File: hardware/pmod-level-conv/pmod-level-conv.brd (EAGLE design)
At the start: 23 x 18.5 mm, 6 parts, among them J1 PMOD_PLUG1, J2 PMOD_SOCKET1, J3 VCC, U1 TXB0108PWR

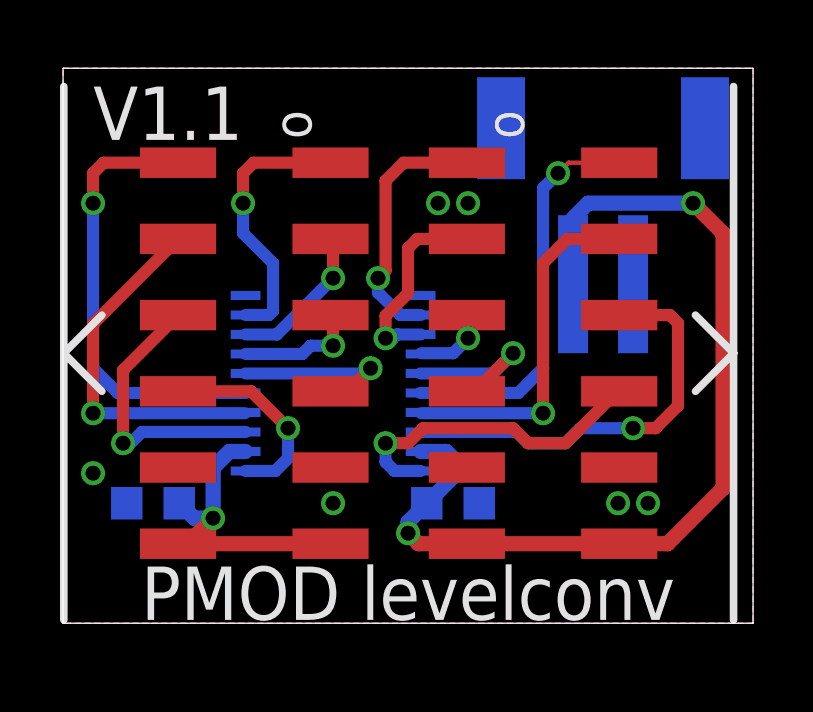
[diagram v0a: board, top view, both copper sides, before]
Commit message: pmod-level-conv : fixed NC OE
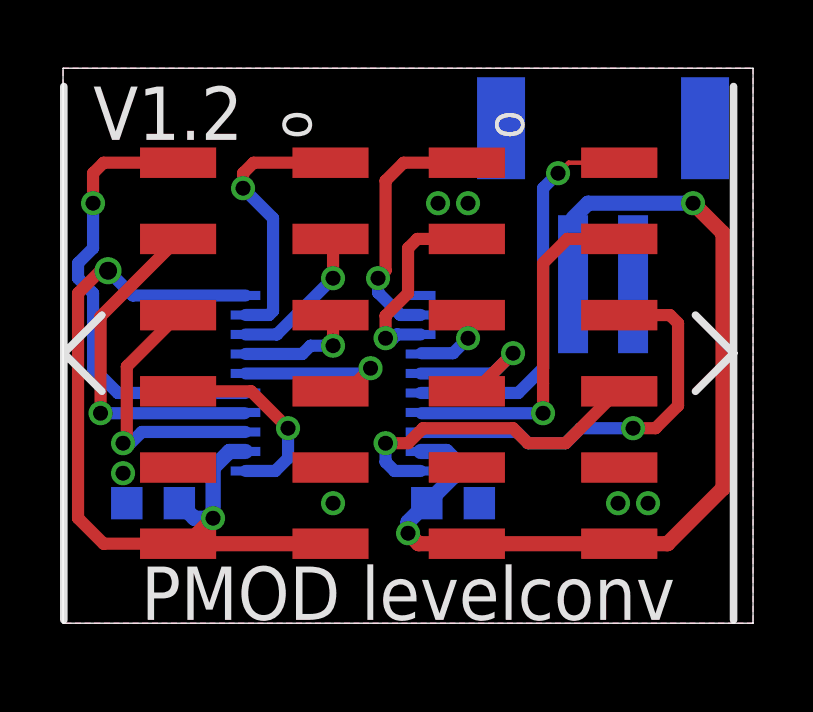
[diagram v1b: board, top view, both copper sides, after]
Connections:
- net VCCIO: now also U1.10
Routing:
- net VCCIO: track 10.9 -> 28.3 mm, vias 1 -> 2
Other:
- board text added: "V1.2"
- board text removed: "V1.1"
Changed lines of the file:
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@@
 <wire x1="0" y1="18.5" x2="0" y2="0" width="0" layer="20"/>
 <text x="11.5" y="1" size="1.778" layer="21" font="vector" align="center">PMOD levelconv</text>
-<text x="3.5" y="17" size="1.778" layer="21" font="vector" align="center">V1.1</text>
+<text x="3.5" y="17" size="1.778" layer="21" font="vector" align="center">V1.2</text>
 </plain>
 <attributes>
@@
 <vertex x="0" y="0"/>
 </polygon>
-<via x="1" y="5" extent="1-16" drill="0.5" shape="octagon"/>
+<via x="2" y="5" extent="1-16" drill="0.5" shape="octagon"/>
 <via x="9" y="4" extent="1-16" drill="0.5" shape="octagon"/>
 <via x="19.5" y="4" extent="1-16" drill="0.5" shape="octagon"/>
@@
 <wire x1="5" y1="3.5" x2="5" y2="5.1793125" width="0.508" layer="16"/>
 <wire x1="5.5456875" y1="5.725" x2="6.0822" y2="5.725" width="0.508" layer="16"/>
+<contactref element="U1" pad="10"/>
+<wire x1="6.0822" y1="10.925" x2="2.325" y2="10.925" width="0.4064" layer="16"/>
+<wire x1="2.325" y1="10.925" x2="1.5" y2="11.75" width="0.4064" layer="16"/>
+<via x="1.5" y="11.75" extent="1-16" drill="0.6" shape="octagon"/>
+<wire x1="1.5" y1="11.75" x2="1.25" y2="11.75" width="0.4064" layer="1"/>
+<wire x1="1.25" y1="11.75" x2="0.5" y2="11" width="0.4064" layer="1"/>
+<wire x1="0.5" y1="11" x2="0.5" y2="3.5" width="0.4064" layer="1"/>
+<wire x1="3.835" y1="2.65" x2="1.35" y2="2.65" width="0.4064" layer="1"/>
+<wire x1="1.35" y1="2.65" x2="0.5" y2="3.5" width="0.4064" layer="1"/>
 </signal>
 <signal name="VCC">
@@
 <wire x1="6.0822" y1="6.375" x2="2.625" y2="6.375" width="0.4064" layer="16"/>
 <via x="2" y="6" extent="1-16" drill="0.5" shape="octagon"/>
-<wire x1="2" y1="6" x2="2" y2="8.435" width="0.4064" layer="1"/>
-<wire x1="2" y1="8.435" x2="3.835" y2="10.27" width="0.4064" layer="1"/>
+<wire x1="2" y1="6" x2="2.125" y2="6.125" width="0.4064" layer="1"/>
+<wire x1="2.125" y1="6.125" x2="2.125" y2="8.56" width="0.4064" layer="1"/>
+<wire x1="2.125" y1="8.56" x2="3.835" y2="10.27" width="0.4064" layer="1"/>
 <wire x1="2.625" y1="6.375" x2="2.25" y2="6" width="0.4064" layer="16"/>
 <wire x1="2.25" y1="6" x2="2" y2="6" width="0.15" layer="16"/>
@@
 <contactref element="U1" pad="4"/>
 <contactref element="J1" pad="8"/>
-<wire x1="3.835" y1="12.81" x2="1" y2="9.975" width="0.4064" layer="1"/>
-<wire x1="1" y1="9.975" x2="1" y2="7" width="0.4064" layer="1"/>
-<via x="1" y="7" extent="1-16" drill="0.5" shape="octagon"/>
-<wire x1="1" y1="7" x2="6.0572" y2="7" width="0.4064" layer="16"/>
+<wire x1="3.835" y1="12.81" x2="1.25" y2="10.225" width="0.4064" layer="1"/>
+<wire x1="1.25" y1="10.225" x2="1.25" y2="7" width="0.4064" layer="1"/>
+<via x="1.25" y="7" extent="1-16" drill="0.5" shape="octagon"/>
+<wire x1="1.25" y1="7" x2="6.0572" y2="7" width="0.4064" layer="16"/>
 <wire x1="6.0572" y1="7" x2="6.0822" y2="7.025" width="0.15" layer="16"/>
 </signal>
@@
 <wire x1="1" y1="15" x2="1" y2="14" width="0.4064" layer="1"/>
 <via x="1" y="14" extent="1-16" drill="0.5" shape="octagon"/>
-<wire x1="1" y1="14" x2="1" y2="8.5" width="0.4064" layer="16"/>
+<wire x1="1" y1="14" x2="1" y2="12.5" width="0.4064" layer="16"/>
+<wire x1="1" y1="12.5" x2="0.5" y2="12" width="0.4064" layer="16"/>
+<wire x1="0.5" y1="12" x2="0.5" y2="11.5" width="0.4064" layer="16"/>
+<wire x1="0.5" y1="11.5" x2="1" y2="11" width="0.4064" layer="16"/>
+<wire x1="1" y1="11" x2="1" y2="8.5" width="0.4064" layer="16"/>
 <wire x1="1" y1="8.5" x2="1.825" y2="7.675" width="0.4064" layer="16"/>
 <wire x1="1.825" y1="7.675" x2="6.0822" y2="7.675" width="0.4064" layer="16"/>
@@
 <wire x1="8.915" y1="15.35" x2="6.35" y2="15.35" width="0.4064" layer="1"/>
 <wire x1="6.35" y1="15.35" x2="6" y2="15" width="0.4064" layer="1"/>
-<wire x1="6" y1="15" x2="6" y2="14" width="0.4064" layer="1"/>
-<via x="6" y="14" extent="1-16" drill="0.5" shape="octagon"/>
-<wire x1="6" y1="14" x2="6" y2="13" width="0.4064" layer="16"/>
-<wire x1="6" y1="13" x2="7" y2="12" width="0.4064" layer="16"/>
+<wire x1="6" y1="15" x2="6" y2="14.5" width="0.4064" layer="1"/>
+<via x="6" y="14.5" extent="1-16" drill="0.5" shape="octagon"/>
+<wire x1="6" y1="14.5" x2="7" y2="13.5" width="0.4064" layer="16"/>
 <wire x1="7" y1="10.40943125" x2="6.86556875" y2="10.275" width="0.4064" layer="16"/>
-<wire x1="7" y1="12" x2="7" y2="10.40943125" width="0.4064" layer="16"/>
+<wire x1="7" y1="13.5" x2="7" y2="10.40943125" width="0.4064" layer="16"/>
 <wire x1="6.86556875" y1="10.275" x2="6.0822" y2="10.275" width="0.4064" layer="16"/>
 </signal>
